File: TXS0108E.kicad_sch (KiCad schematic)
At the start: 17 parts, among them J48 logic_convert, Q5 Q_NPN_BCE, Q6 FDN306P, Q7 Q_NPN_BCE, Q8 FDN306P, Q9 2N7002, U8 TXS0108EPW

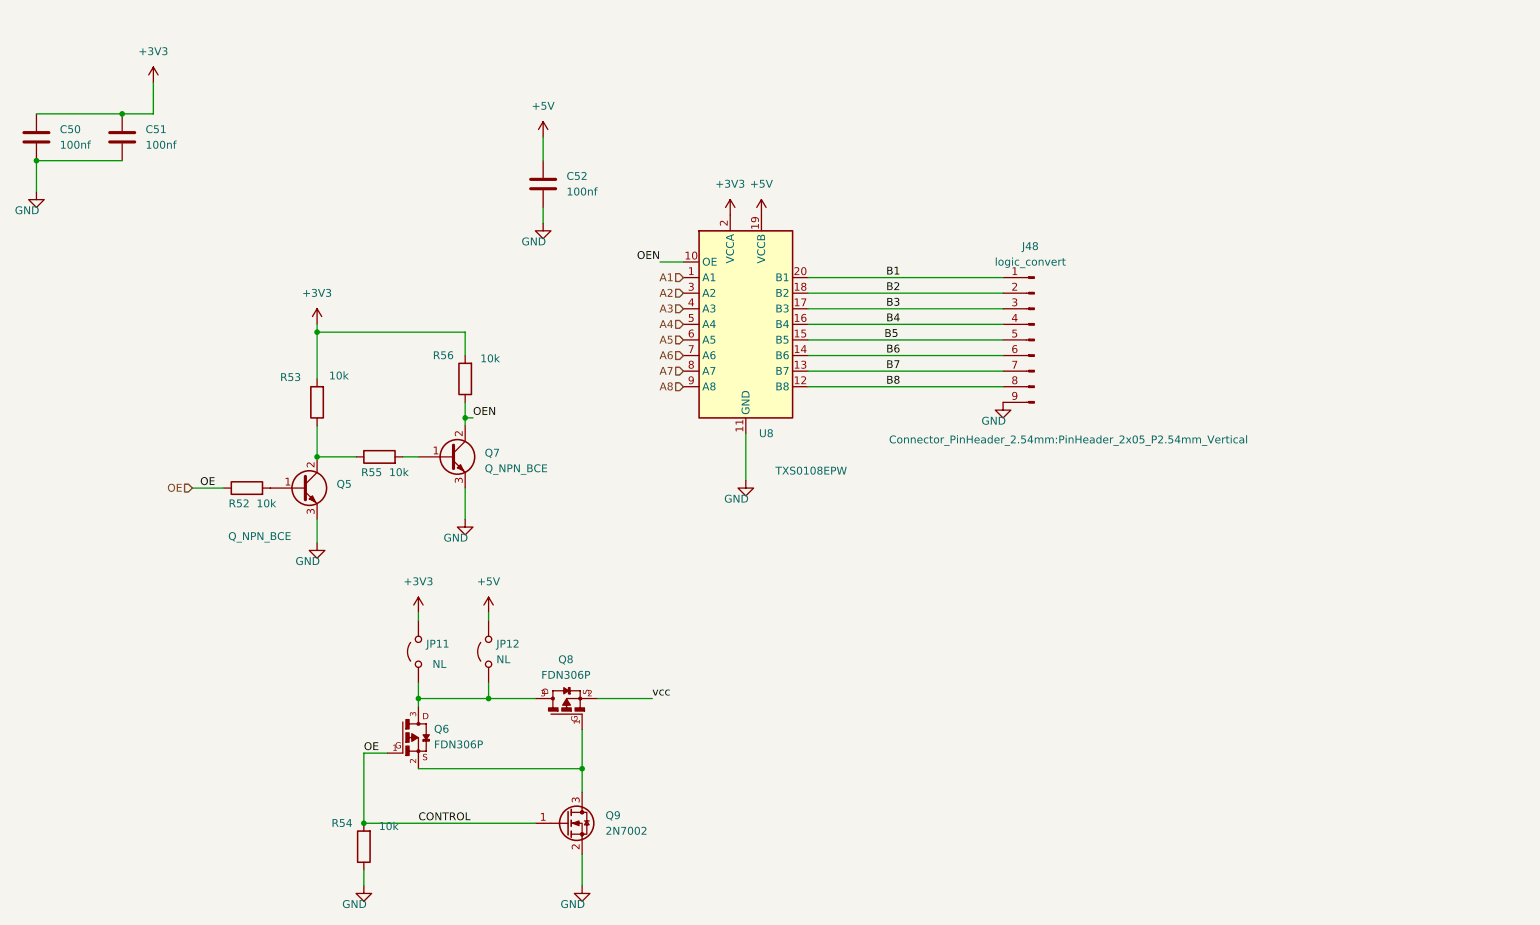
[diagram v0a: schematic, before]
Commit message: se agrego osciloscoio
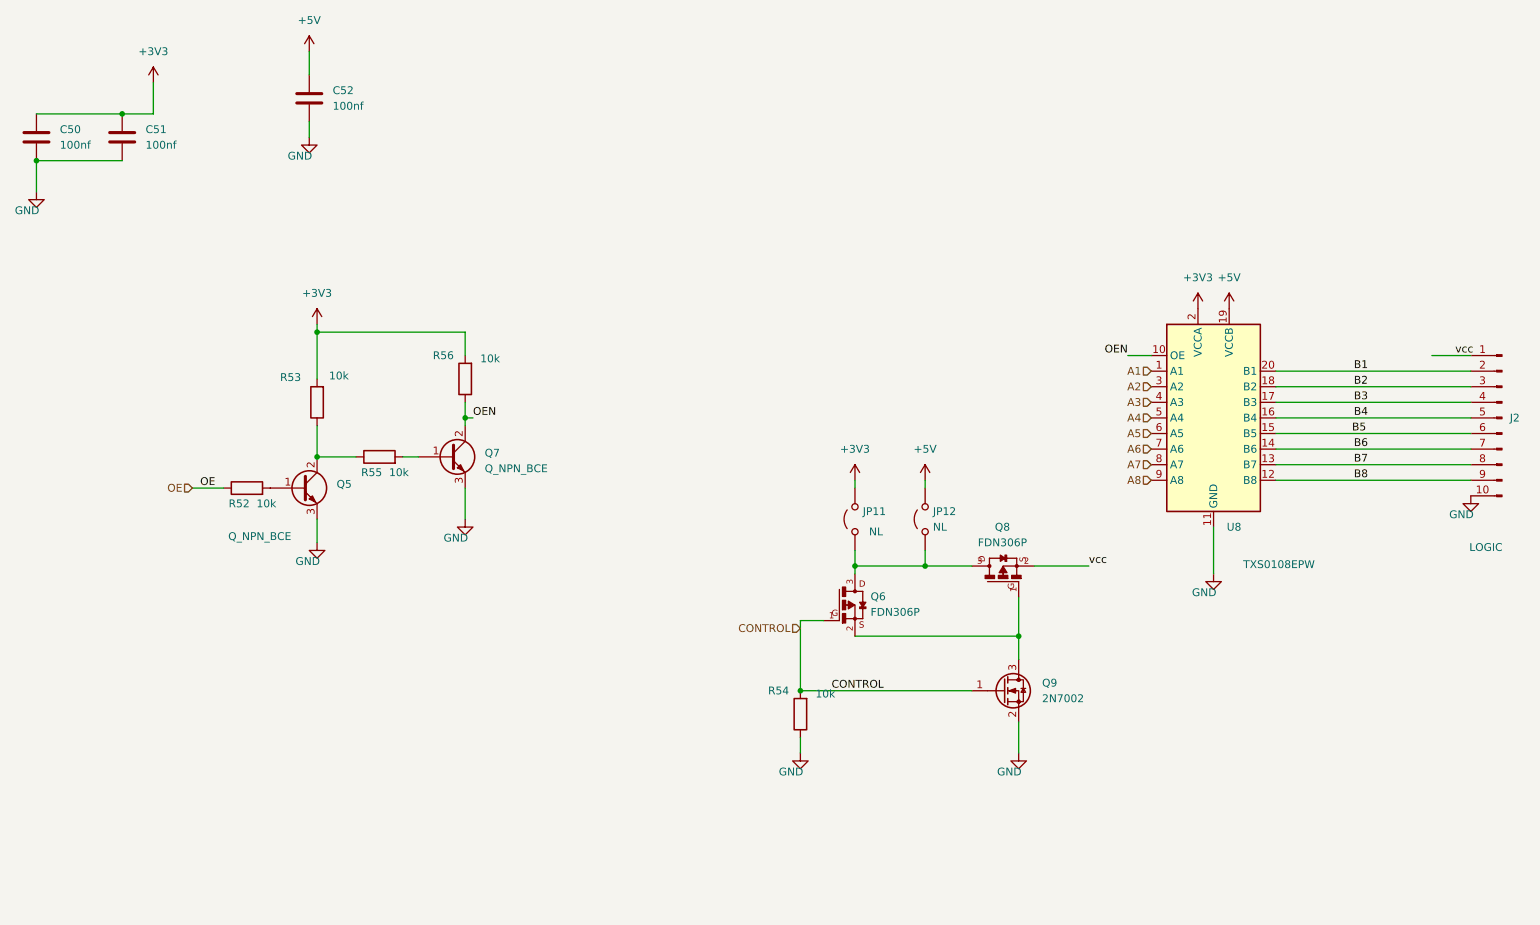
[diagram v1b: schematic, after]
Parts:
- removed J48: logic_convert, Connector_PinHeader_2.54mm:PinHeader_2x05_P2.54mm_Vertical, symbol Connector:Conn_01x09_Pin
- added J2: LOGIC, Connector_PinHeader_2.54mm:PinHeader_1x10_P2.54mm_Vertical, symbol Connector:Conn_01x10_Pin
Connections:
- net B1: now also J2.2 (Pin_2)
- net B2: now also J2.3 (Pin_3)
- net B3: now also J2.4 (Pin_4)
- net B4: now also J2.5 (Pin_5)
- net B5: now also J2.6 (Pin_6)
- net B6: now also J2.7 (Pin_7)
- net B7: now also J2.8 (Pin_8)
- net B8: now also J2.9 (Pin_9)
- net GND: now also J2.10 (Pin_10)
- net OE: no longer Q6.1, Q9.1 (G), R54.2
- net vcc: now also J2.1 (Pin_1)
- new net CONTROL: Q6.1, Q9.1 (G), R54.2
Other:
- moved on the sheet: C52, JP11, JP12, Q6, Q8, Q9, R54, U8
